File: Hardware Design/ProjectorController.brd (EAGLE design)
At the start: 39 x 34.9 mm, 18 parts, among them J1 5747844-4, J2 Cap Buttons, J3 Prog, J4 Prog/Run, J5 10118194-0001LF, U1 ESP-WROOM-32, U2 SP3232EEN-L

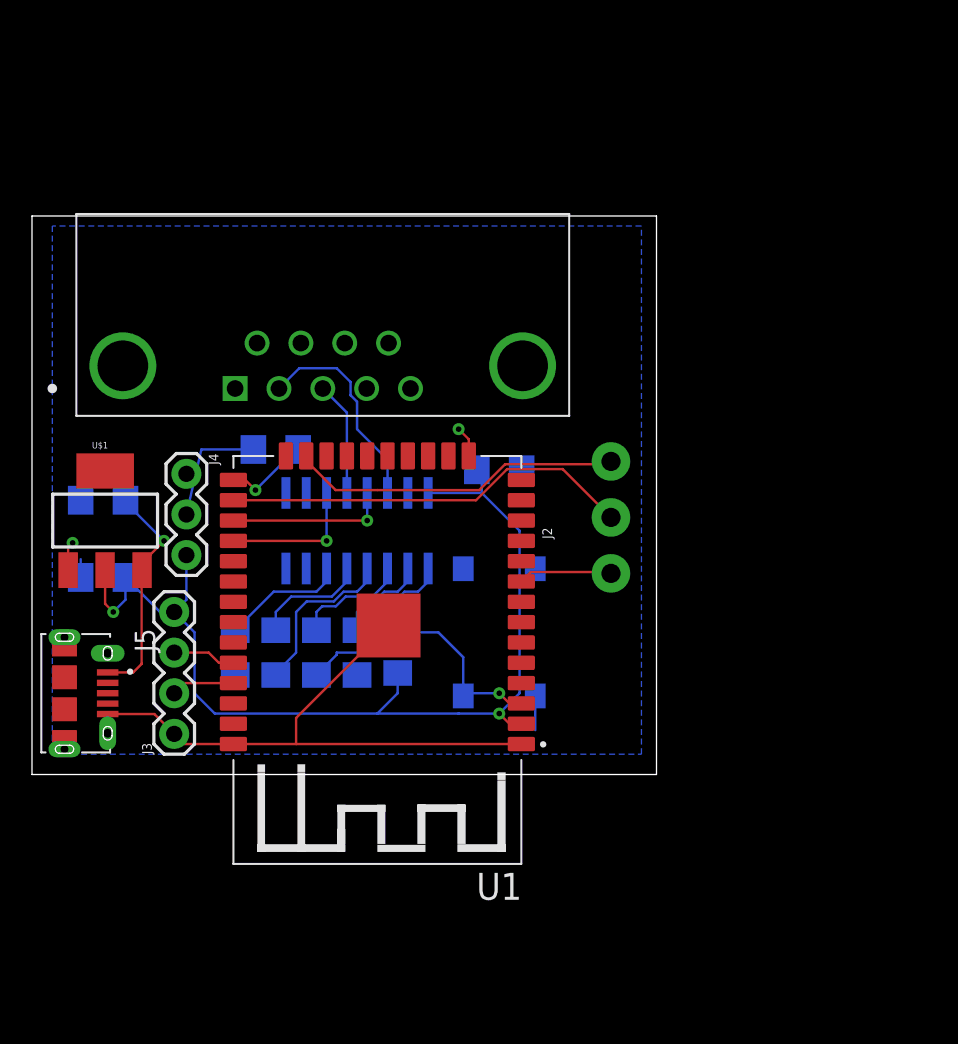
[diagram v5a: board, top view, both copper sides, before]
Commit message: Revert "ED-33 Major board redesign to make smaller"
This reverts commit ff5836e82a7b4c6ccf7f1796d2610aee96480eab.
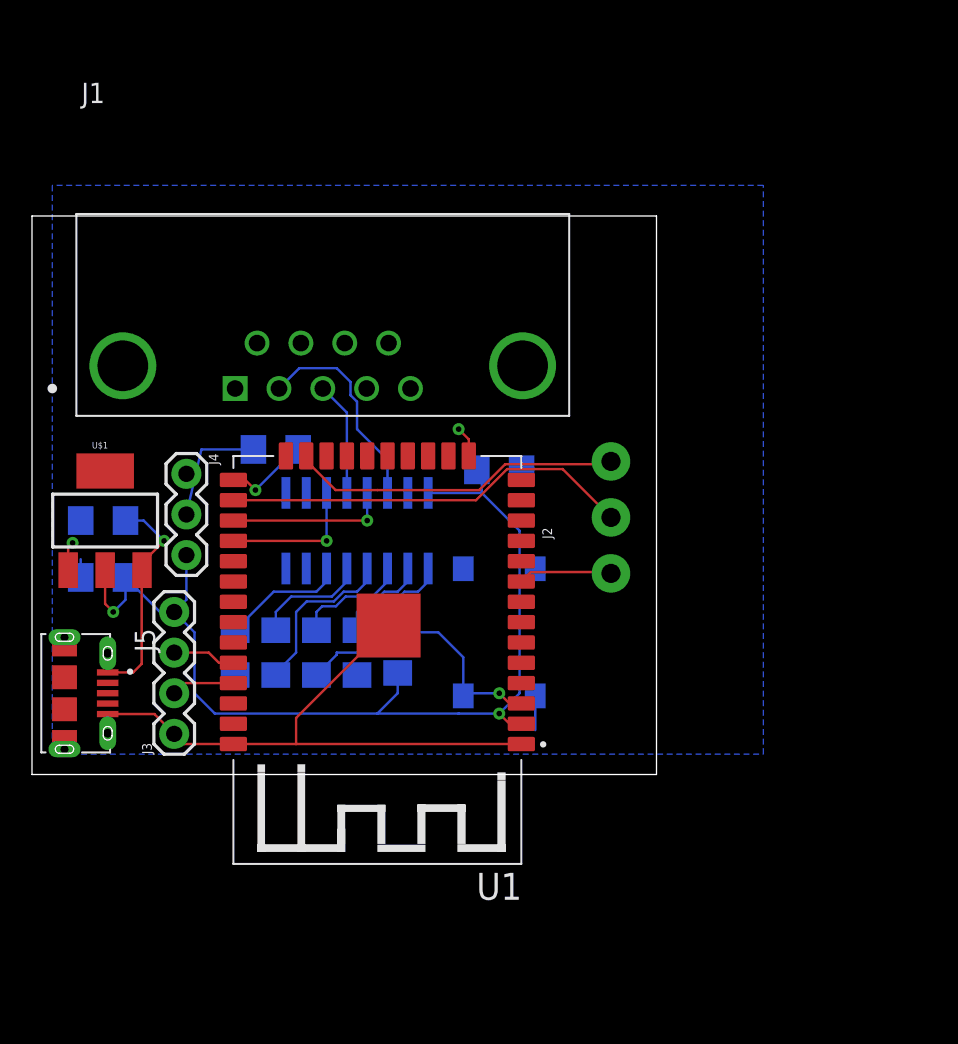
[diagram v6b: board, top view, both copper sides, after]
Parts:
- moved C2 1.27 mm to (8.26, 59.1)
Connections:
- net GND: no longer J5.S1, J5.S2, J5.S3, J5.S4, J5.S5, J5.S6
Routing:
- net 5V: track 14.2 -> 13.6 mm
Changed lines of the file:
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@@
 <?xml version="1.0" encoding="utf-8"?>
 <!DOCTYPE eagle SYSTEM "eagle.dtd">
-<eagle version="9.6.1">
+<eagle version="9.5.2">
 <drawing>
 <settings>
@@
 <attribute name="VALUE" x="8.255" y="54.356" size="0.6096" layer="28" font="vector" ratio="20" rot="MR0" align="top-center"/>
 </element>
-<element name="C2" library="SparkFun-Capacitors" package="1206" value="10uF" x="8.255" y="60.325" smashed="yes" rot="MR0">
-<attribute name="NAME" x="8.255" y="61.468" size="0.6096" layer="26" font="vector" ratio="20" rot="MR0" align="bottom-center"/>
-<attribute name="VALUE" x="8.255" y="59.182" size="0.6096" layer="28" font="vector" ratio="20" rot="MR0" align="top-center"/>
+<element name="C2" library="SparkFun-Capacitors" package="1206" value="10uF" x="8.255" y="59.055" smashed="yes" rot="MR0">
+<attribute name="NAME" x="8.255" y="60.198" size="0.6096" layer="26" font="vector" ratio="20" rot="MR0" align="bottom-center"/>
+<attribute name="VALUE" x="8.255" y="57.912" size="0.6096" layer="28" font="vector" ratio="20" rot="MR0" align="top-center"/>
 </element>
 <element name="J1" library="5747844-4" package="TE_5747844-4" value="5747844-4" x="16.51" y="67.31" smashed="yes">
@@
 <attribute name="MF" value="TE Connectivity" x="54.61" y="29.21" size="1.778" layer="27" display="off"/>
 <attribute name="MP" value="5747844-4" x="54.61" y="29.21" size="1.778" layer="27" display="off"/>
+<attribute name="NAME" x="6.90275" y="85.152" size="1.27228125" layer="25"/>
 <attribute name="NUMBER_OF_POSITIONS" value="9" x="54.61" y="29.21" size="1.778" layer="27" display="off"/>
 <attribute name="PACKAGE" value="None" x="54.61" y="29.21" size="1.778" layer="27" display="off"/>
@@
 <element name="J2" library="SparkFun-Connectors" package="SCREWTERMINAL-3.5MM-3-NS" value="Cap Buttons" x="40.005" y="55.753" smashed="yes" rot="R90">
 <attribute name="NAME" x="36.322" y="57.912" size="0.6096" layer="25" font="vector" ratio="20" rot="R90"/>
-<attribute name="VALUE" x="38.227" y="57.785" size="0.6096" layer="27" font="vector" ratio="20" rot="R90"/>
+<attribute name="VALUE" x="44.577" y="57.785" size="0.6096" layer="27" font="vector" ratio="20" rot="R90"/>
 </element>
 <element name="J3" library="SparkFun-Connectors" package="1X04" value="Prog" x="12.7" y="45.72" smashed="yes" rot="R90">
@@
 <attribute name="PACKAGE" value="None" x="5.842" y="48.26" size="1.778" layer="27" rot="R270" display="off"/>
 <attribute name="PRICE" value="None" x="5.842" y="48.26" size="1.778" layer="27" rot="R270" display="off"/>
+<attribute name="VALUE" x="1.122040625" y="52.72785" size="1.270459375" layer="27" rot="R270"/>
 </element>
 <element name="C3" library="SparkFun-Capacitors" package="1206" value="0.1uF" x="33.02" y="62.23" smashed="yes" rot="MR0">
@@
 <contactref element="C7" pad="1"/>
 <polygon width="0.1524" layer="16">
-<vertex x="5.08" y="77.47"/>
+<vertex x="5.08" y="80.01"/>
 <vertex x="5.08" y="44.45"/>
-<vertex x="41.91" y="44.45"/>
-<vertex x="41.91" y="77.47"/>
+<vertex x="49.53" y="44.45"/>
+<vertex x="49.53" y="80.01"/>
 </polygon>
 <wire x1="6.855" y1="56.639" x2="6.855" y2="55.499" width="0.1524" layer="16"/>
@@
 <wire x1="6.0706" y1="55.9562" x2="6.0706" y2="57.3786" width="0.1524" layer="1"/>
 <wire x1="6.0706" y1="57.3786" x2="6.35" y2="57.658" width="0.1524" layer="1"/>
-<contactref element="J5" pad="S3"/>
-<contactref element="J5" pad="S6"/>
-<contactref element="J5" pad="S1"/>
-<contactref element="J5" pad="S2"/>
-<contactref element="J5" pad="S5"/>
-<contactref element="J5" pad="S4"/>
-<wire x1="5.842" y1="47.26" x2="5.842" y2="49.26" width="0" layer="19" extent="1-1"/>
-<wire x1="5.842" y1="51.76" x2="5.842" y2="49.26" width="0" layer="19" extent="1-1"/>
 </signal>
 <signal name="3V3">
@@
 <wire x1="10.665" y1="55.9278" x2="10.6934" y2="55.9562" width="0.1524" layer="1"/>
 <wire x1="8.542" y1="49.56" x2="8.572" y2="49.53" width="0.1524" layer="1"/>
-<wire x1="9.655" y1="60.325" x2="9.655" y2="60.195" width="0.1524" layer="16"/>
-<wire x1="12.065" y1="57.785" x2="9.655" y2="60.195" width="0.1524" layer="16"/>
+<wire x1="9.655" y1="59.055" x2="10.795" y2="59.055" width="0.1524" layer="16"/>
+<wire x1="12.065" y1="57.785" x2="10.795" y2="59.055" width="0.1524" layer="16"/>
 <via x="12.065" y="57.785" extent="1-16" drill="0.35"/>
 <wire x1="10.6934" y1="55.9562" x2="10.6934" y2="56.4134" width="0.1524" layer="1"/>
 <wire x1="12.065" y1="57.785" x2="10.6934" y2="56.4134" width="0.1524" layer="1"/>
-<wire x1="8.542" y1="49.56" x2="10.13" y2="49.56" width="0.1524" layer="1" locked="yes"/>
+<wire x1="8.542" y1="49.56" x2="10.13" y2="49.56" width="0.1524" layer="1"/>
 <wire x1="10.13" y1="49.56" x2="10.665" y2="50.095" width="0.1524" layer="1"/>
 <wire x1="10.665" y1="50.095" x2="10.665" y2="55.9278" width="0.1524" layer="1"/>
@@
 </board>
 </drawing>
-<compatibility>
-<note version="8.5" severity="warning">
-Since Version 8.5, EAGLE supports locking for holes, vias, wires and polygons.
-The locking property on all objects of these types will not be understood in this version.
-</note>
-</compatibility>
 </eagle>
